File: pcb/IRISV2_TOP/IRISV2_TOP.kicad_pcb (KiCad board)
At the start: 2 copper layers, 50 x 50 mm, 140 parts, among them IC1 ATA6561-GAQW-N, IC2 S25FL256LAGNFI010, IC3 STM32C552MET6, J2 USB_C_Receptacle_USB2.0_16P, J3 USB_C_Receptacle_USB2.0_16P, U4 STM32H563VITx, U5 MMC5983MA, U6 ICM-45686, U7 ICM-45686, U8 BMP581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

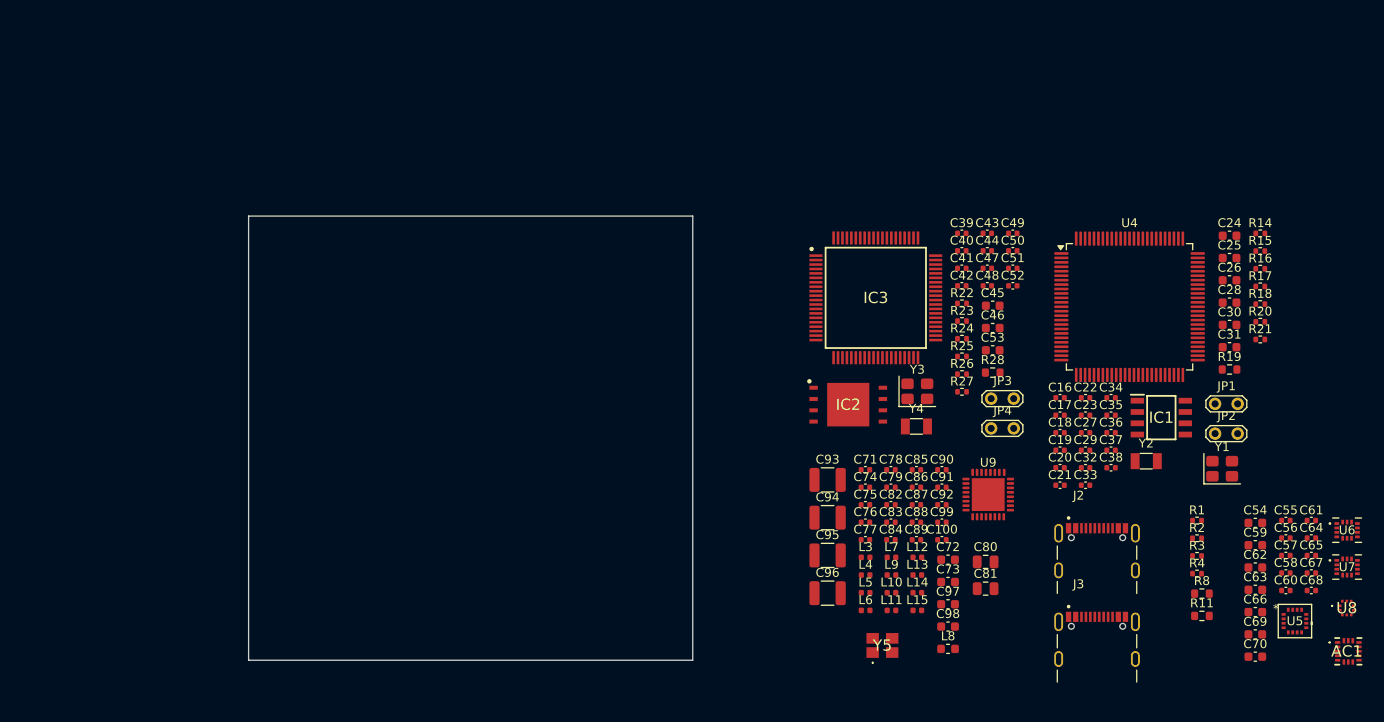
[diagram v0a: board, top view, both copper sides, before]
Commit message: gps finished minus tvs (WHY ARE THEY ALL 0201), top layout + routing started
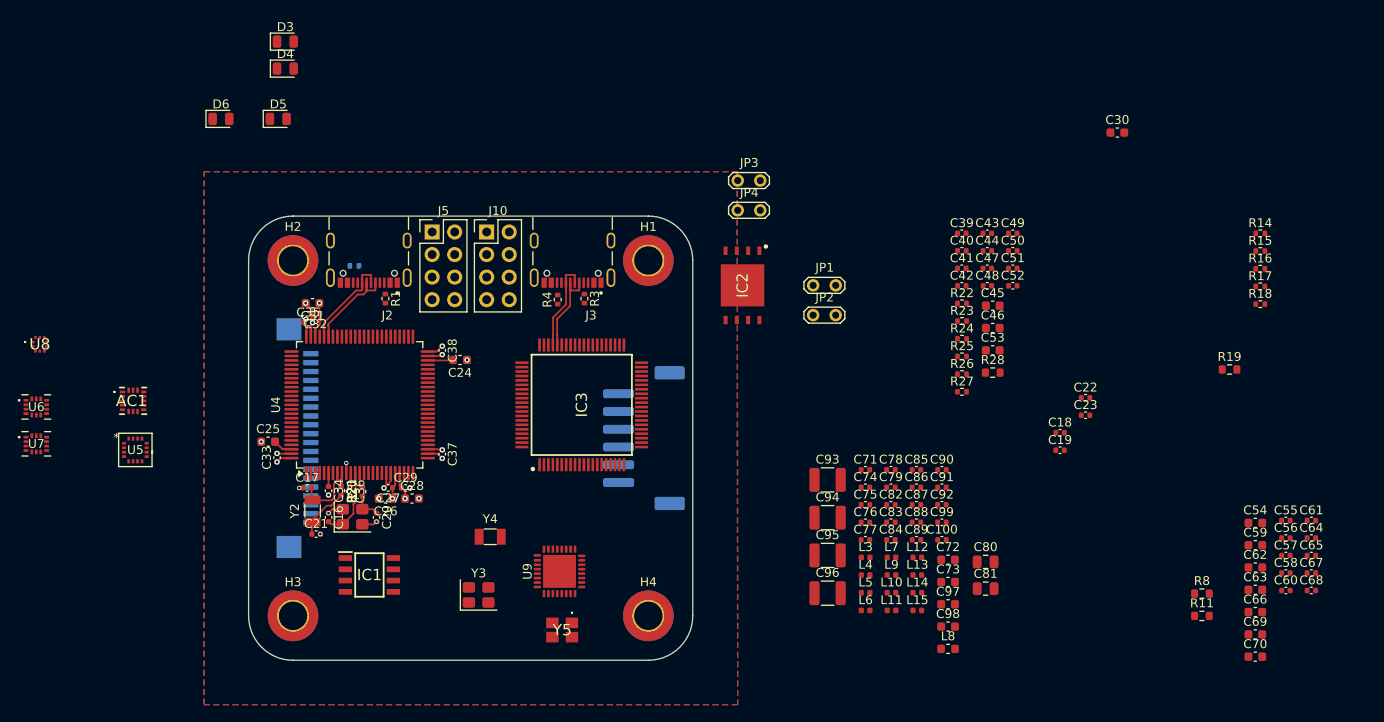
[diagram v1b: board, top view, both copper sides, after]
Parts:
- added D3: 3.3_GOOD, LED_SMD:LED_0805_2012Metric, F.Cu at (129.1, 55.4)
- added D4: 5_GOOD, LED_SMD:LED_0805_2012Metric, F.Cu at (129.1, 58.4)
- added D5: STATUS, LED_SMD:LED_0805_2012Metric, F.Cu at (128.3, 64.1)
- added D6: STATUS, LED_SMD:LED_0805_2012Metric, F.Cu at (121.9, 64.1)
- added H1: MountingHole_Pad, MountingHole:MountingHole_3.2mm_M3_ISO7380_Pad_TopBottom, F.Cu at (170.0, 80.0)
- added H2: MountingHole_Pad, MountingHole:MountingHole_3.2mm_M3_ISO7380_Pad_TopBottom, F.Cu at (130.0, 80.0)
- added H3: MountingHole_Pad, MountingHole:MountingHole_3.2mm_M3_ISO7380_Pad_TopBottom, F.Cu at (130.0, 120.0)
- added H4: MountingHole_Pad, MountingHole:MountingHole_3.2mm_M3_ISO7380_Pad_TopBottom, F.Cu at (170.0, 120.0)
- added J1: Conn_01x20_MountingPin, FFC3B07-20-T:FFC3B07-20-T, B.Cu at (132.0, 100.0)
- added J10: Conn_02x04_Odd_Even, Connector_PinHeader_2.54mm:PinHeader_2x04_P2.54mm_Vertical, F.Cu at (151.8, 76.8)
- added J5: Conn_02x04_Odd_Even, Connector_PinHeader_2.54mm:PinHeader_2x04_P2.54mm_Vertical, F.Cu at (145.7, 76.8)
- added J9: Conn_01x06_MountingPin, Connector_JST:JST_PH_S6B-PH-SM4-TB_1x06-1MP_P2.00mm_Horizontal, B.Cu at (169.5, 100.0)
- R2: moved to B.Cu
- moved U8 150.1 mm to (101.5, 89.4)
- moved U6 148.2 mm to (101.1, 96.5)
- moved U7 148.2 mm to (101.1, 100.6)
- moved AC1 139.7 mm to (112.0, 95.8)
- moved U5 132.0 mm to (112.2, 101.3)
- moved C25 110.2 mm to (127.2, 100.4)
- moved R21 104.9 mm to (135.4, 105.9), turned to -90 degrees
- moved C31 103.3 mm to (132.2, 84.8), turned to 180 degrees
- moved R20 102.9 mm to (137.8, 106.0), turned to 90 degrees
- moved R2 99.7 mm to (136.9, 80.6)
- moved C26 98.1 mm to (140.4, 106.8), turned to 180 degrees
- moved Y1 98.0 mm to (136.7, 108.8)
- moved R1 94.7 mm to (140.4, 84.3), turned to -90 degrees
- moved C28 94.6 mm to (143.4, 106.8)
- moved Y2 94.0 mm to (132.2, 108.2), turned to 90 degrees
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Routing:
- net +3.3V: track 0.00 -> 21.8 mm, vias 0 -> 8
- net GND: track 0.00 -> 20.8 mm, vias 0 -> 18
- net usb1_d+: track 0.00 -> 10.9 mm
- net usb1_d-: track 0.00 -> 10.9 mm
- net usb2_d+: track 0.00 -> 10.3 mm
- net usb2_d-: track 0.00 -> 10.3 mm
- net /main_mcu/hse_0: track 0.00 -> 8.12 mm
- net /main_mcu/lse_0: track 0.00 -> 6.91 mm
- net /main_mcu/lse_1: track 0.00 -> 6.49 mm
- net Net-(C24-Pad2): track 0.00 -> 5.07 mm
- net /main_mcu/hse_1: track 0.00 -> 3.27 mm
- net Net-(U4-PH1): track 0.00 -> 1.69 mm
- net Net-(U4-PC15): track 0.00 -> 1.52 mm
- added copper zone on In2.Cu, net +3.3V
- added copper zone on B.Cu, net GND
- added copper zone on F.Cu, net GND
- added copper zone on In1.Cu, net GND
- added copper zone on In4.Cu, net GND
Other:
- outline, holes or cut-outs redrawn
- copper layers 2 -> 6

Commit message: removed high g accel, top board layout looking decent, routing started also - though i realized i was missing the micro sd card and that's going to be a pain to add
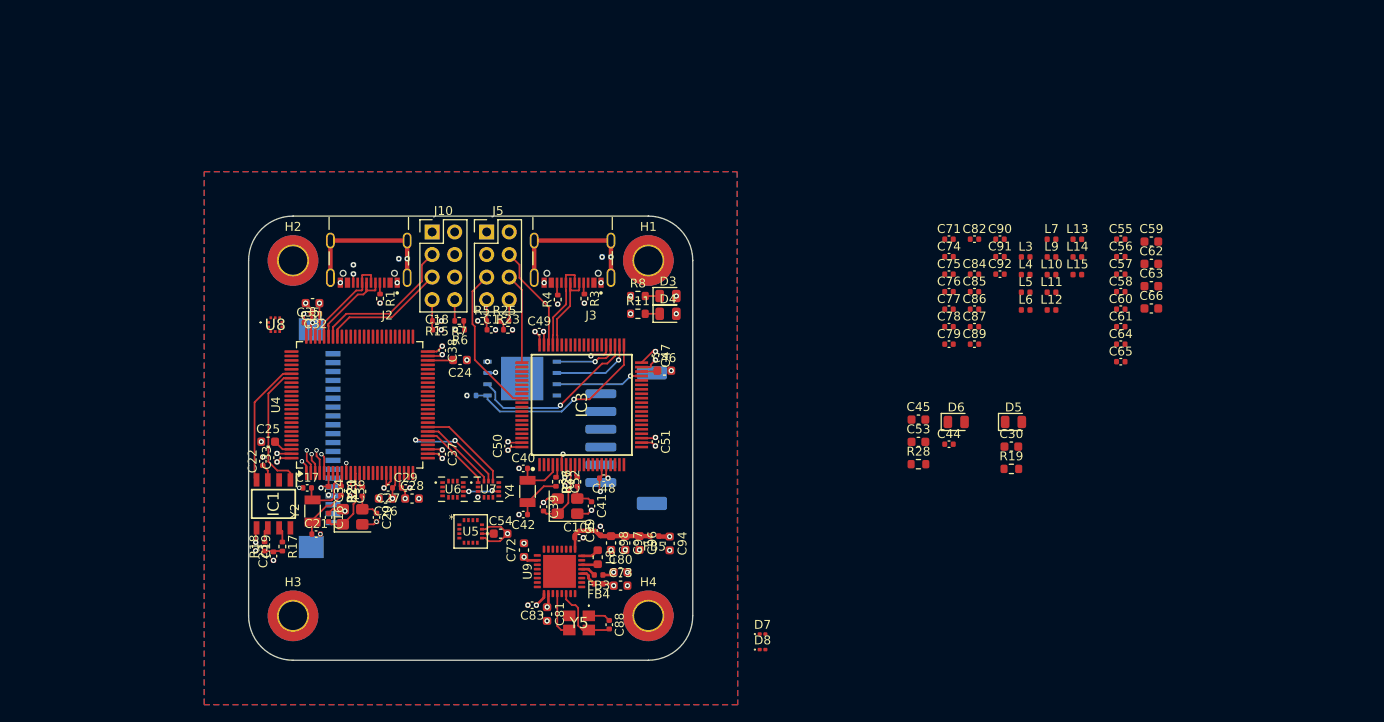
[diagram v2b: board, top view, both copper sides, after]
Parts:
- removed AC1: H3LIS331DLTR, H3LIS331DLTR:LIS3DHTR
- removed C43, C67, C68: 100nF, Capacitor_SMD:C_0402_1005Metric
- removed C69, C70: 10uF, Capacitor_SMD:C_0603_1608Metric
- removed C93, C95: 22uF, Capacitor_SMD:C_1210_3225Metric
- removed JP1, JP3: BOOT, TestPoint:TestPoint_2Pads_Pitch2.54mm_Drill0.8mm
- removed JP2, JP4: RST, TestPoint:TestPoint_2Pads_Pitch2.54mm_Drill0.8mm
- removed R14, R16, R24: 10k, Resistor_SMD:R_0402_1005Metric
- added C1: 100nF, Capacitor_SMD:C_0402_1005Metric, F.Cu at (152.3, 87.8)
- added D7: D_TVS, Diode_SMD:D_0201_0603Metric, F.Cu at (182.9, 122.0)
- added D8: D_TVS, Diode_SMD:D_0201_0603Metric, F.Cu at (182.9, 123.8)
- added FB1: FerriteBead_Small, Inductor_SMD:L_0402_1005Metric, B.Cu at (142.4, 79.8)
- added FB2: FerriteBead_Small, Inductor_SMD:L_0402_1005Metric, B.Cu at (165.3, 79.6)
- added FB3: FerriteBead_Small, Inductor_SMD:L_0402_1005Metric, F.Cu at (164.4, 115.4)
- added FB4: FerriteBead_Small, Inductor_SMD:L_0402_1005Metric, F.Cu at (164.4, 116.4)
- added FB5: FerriteBead_Small, Inductor_SMD:L_0402_1005Metric, F.Cu at (170.7, 111.0)
- added R5: 10k, Resistor_SMD:R_0402_1005Metric, F.Cu at (151.3, 86.8)
- added R6: 10k, Resistor_SMD:R_0402_1005Metric, F.Cu at (148.8, 87.8)
- added R7: 10k, Resistor_SMD:R_0402_1005Metric, F.Cu at (148.7, 86.8)
- C80, C81: footprint Capacitor_SMD:C_0805_2012Metric -> Capacitor_SMD:C_0603_1608Metric
- C94: value 22uF -> 1uF; footprint Capacitor_SMD:C_1210_3225Metric -> Capacitor_SMD:C_0603_1608Metric
- C96: value 22uF -> 10uF; footprint Capacitor_SMD:C_1210_3225Metric -> Capacitor_SMD:C_0603_1608Metric
- IC2, R22: moved to B.Cu
- moved R18 115.4 mm to (126.8, 112.2), turned to 90 degrees
- moved R17 113.9 mm to (128.8, 112.2), turned to -90 degrees
- moved R15 93.0 mm to (146.2, 86.8), turned to 180 degrees
- moved C22 92.9 mm to (126.6, 102.6), turned to 90 degrees
- moved C23 92.8 mm to (127.8, 113.3), turned to 90 degrees
- moved C19 91.2 mm to (125.8, 112.2), turned to -90 degrees
- moved D6 89.5 mm to (204.7, 98.2)
- moved D5 89.5 mm to (211.1, 98.2)
- moved C54 85.0 mm to (153.4, 110.8)
- moved R11 72.0 mm to (168.8, 86.0)
- moved R8 71.8 mm to (168.8, 84.0)
- moved C18 71.1 mm to (146.2, 87.8)
- moved C50 60.9 mm to (154.2, 100.9), turned to 90 degrees
- moved C39 56.3 mm to (158.2, 107.7), turned to -90 degrees
- moved R22 56.2 mm to (150.1, 95.2)
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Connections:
- IC3 pad 24: unconnected-(IC3-PA4-Pad24) -> lr_nss
- IC3 pad 33: lr_nss -> unconnected-(IC3-PE7-Pad33)
- IC3 pad 37: ppu_i2c2_scl -> /peripheral_mcu/flash_rst
- IC3 pad 41: ppu_i2c2_sda -> /peripheral_mcu/flash_cs
- IC3 pad 45: unconnected-(IC3-PD12-Pad45) -> /peripheral_mcu/flash_wp
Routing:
- net GND: track 20.8 -> 45.1 mm, vias 18 -> 62
- net /peripheral_mcu/flash_cs: track 0.00 -> 22.1 mm, vias 0 -> 1
- net /peripheral_mcu/flash_miso: track 0.00 -> 19.6 mm, vias 0 -> 1
- net /peripheral_mcu/swo: track 0.00 -> 17.2 mm
- net Net-(J3-SHIELD): track 0.00 -> 17.0 mm, vias 0 -> 1
- net Net-(J2-SHIELD): track 0.00 -> 17.0 mm, vias 0 -> 1
- net /main_mcu/debug_uart_rx: track 0.00 -> 16.7 mm
- net /peripheral_mcu/flash_wp: track 0.00 -> 15.3 mm, vias 0 -> 2
- net /main_mcu/can_tx: track 0.00 -> 14.8 mm
- net +3.3V: track 21.8 -> 36.3 mm, vias 8 -> 21
- net /main_mcu/can_rx: track 0.00 -> 14.3 mm
- net /main_mcu/debug_uart_tx: track 0.00 -> 13.9 mm
- net icm2_sck: track 0.00 -> 12.1 mm, vias 0 -> 2
- net /peripheral_mcu/swdio: track 0.00 -> 12.1 mm
- net /lr2021/lr2021_vbat: track 0.00 -> 10.5 mm
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
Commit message: layout pretty much done, lr2021 rf stuff done, mostly just routing left
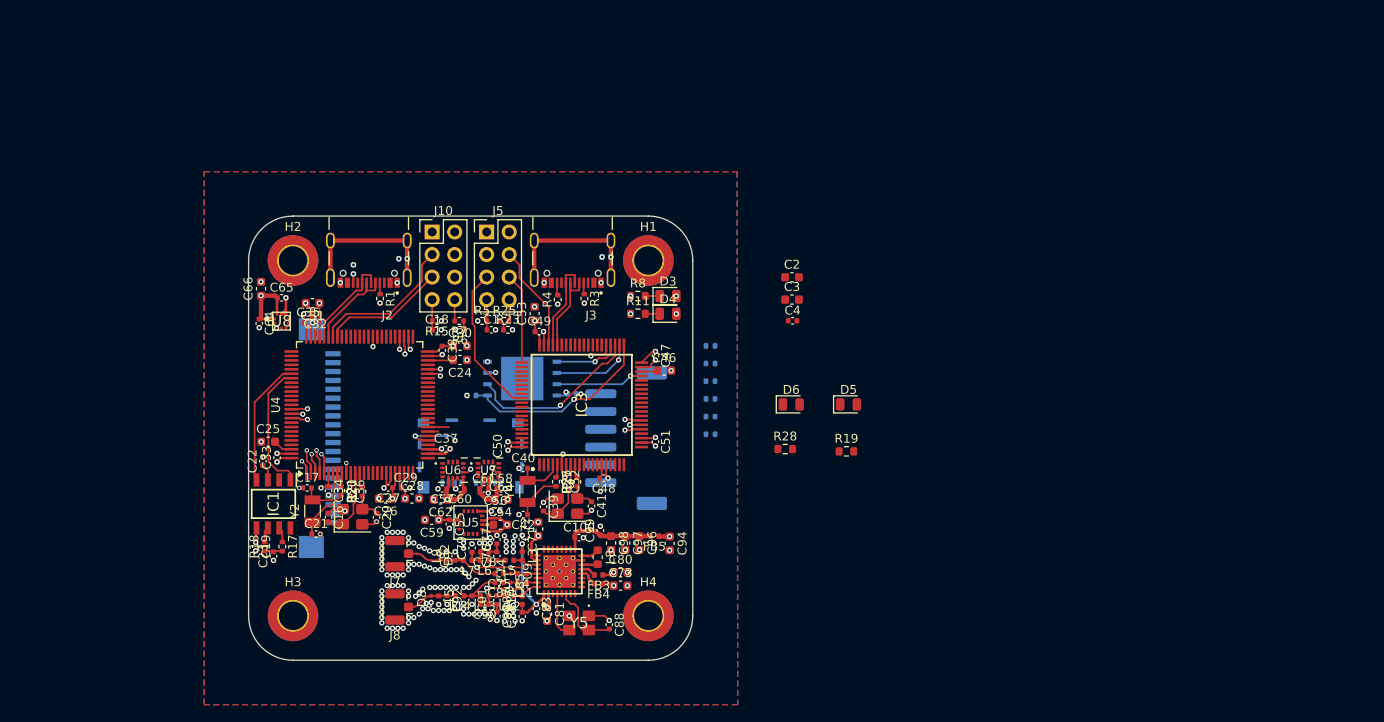
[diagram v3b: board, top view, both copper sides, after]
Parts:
- removed C45: 1uF, Capacitor_SMD:C_0603_1608Metric
- added C2: 10uF, Capacitor_SMD:C_0603_1608Metric, F.Cu at (186.2, 81.9)
- added C3: 1uF, Capacitor_SMD:C_0603_1608Metric, F.Cu at (186.2, 84.4)
- added C4: 100nF, Capacitor_SMD:C_0402_1005Metric, F.Cu at (186.2, 86.8)
- added J6: MEM2085-00-115-00-A, MEM2085-00-115:MEM20850011500A, B.Cu at (150.0, 102.0)
- added J7: Conn_Coaxial, Connector_Coaxial:U.FL_Hirose_U.FL-R-SMT-1_Vertical, F.Cu at (141.9, 113.0)
- added J8: Conn_Coaxial, Connector_Coaxial:U.FL_Hirose_U.FL-R-SMT-1_Vertical, F.Cu at (141.9, 119.0)
- added R10: 10k, Resistor_SMD:R_0402_1005Metric, B.Cu at (177.0, 91.6)
- added R12: 10k, Resistor_SMD:R_0402_1005Metric, B.Cu at (177.0, 93.6)
- added R13: 10k, Resistor_SMD:R_0402_1005Metric, B.Cu at (177.0, 95.6)
- added R14: 10k, Resistor_SMD:R_0402_1005Metric, B.Cu at (177.0, 97.6)
- added R16: 10k, Resistor_SMD:R_0402_1005Metric, B.Cu at (177.0, 99.6)
- added R9: 10k, Resistor_SMD:R_0402_1005Metric, B.Cu at (177.0, 89.6)
- C44: moved to B.Cu
- C74, C85: footprint Capacitor_SMD:C_0402_1005Metric -> Capacitor_SMD:C_0201_0603Metric
- U9: footprint LR2021:LR2021 -> LR2021:LR2021_thermalvias
- moved C66 100.2 mm to (126.4, 83.2), turned to 90 degrees
- moved C64 97.0 mm to (126.2, 87.1), turned to -90 degrees
- moved C65 94.7 mm to (128.7, 84.2)
- moved C59 86.8 mm to (145.6, 109.2), turned to 180 degrees
- moved C62 84.3 mm to (146.6, 106.9), turned to 180 degrees
- moved C55 82.1 mm to (147.6, 109.7), turned to -90 degrees
- moved L15 80.7 mm to (146.4, 118.2), turned to -90 degrees
- moved C57 80.1 mm to (146.8, 105.7), turned to 180 degrees
- moved L14 79.3 mm to (148.8, 117.8), turned to 180 degrees
- moved L13 77.9 mm to (151.6, 117.8), turned to 180 degrees
- moved C60 77.1 mm to (148.8, 105.7), turned to 180 degrees
- moved C63 77.1 mm to (153.4, 106.9)
- moved C56 76.0 mm to (152.8, 108.2)
- moved L9 76.0 mm to (147.3, 113.3), turned to 90 degrees
- moved L7 75.0 mm to (149.7, 113.8), turned to 180 degrees
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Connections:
- net Net-(D7-A2) renamed /lr2021/lf
- C86 pad 2: Net-(D8-A2) -> /lr2021/hf_tiein
- C90 pad 2: Net-(C90-Pad2) -> /lr2021/hf_tiein
- C91 pad 1: Net-(C90-Pad2) -> /lr2021/hf_tiein
- C92 pad 1: Net-(D8-A2) -> /lr2021/hf
- D8 pad 2: Net-(D8-A2) -> /lr2021/hf
- IC3 pad 33: unconnected-(IC3-PE7-Pad33) -> /peripheral_mcu/sd_cs
- L13 pad 2: Net-(C90-Pad2) -> /lr2021/hf_tiein
- L14 pad 1: Net-(C90-Pad2) -> /lr2021/hf_tiein
- L14 pad 2: Net-(D8-A2) -> /lr2021/hf
- L15 pad 1: Net-(D8-A2) -> /lr2021/hf
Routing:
- net mcu->ppu_sck: track 0.00 -> 40.5 mm, vias 0 -> 2
- net mcu->ppu_miso: track 0.00 -> 39.7 mm, vias 0 -> 2
- net mcu->ppu_mosi: track 0.00 -> 39.7 mm, vias 0 -> 2
- net +3.3V: track 36.3 -> 66.7 mm, vias 21 -> 27
- net GND: track 45.1 -> 68.3 mm, vias 62 -> 205
- net /lr2021/lr2021_vdcc: track 2.95 -> 19.3 mm
- net /lr2021/vr_pa: track 1.65 -> 12.8 mm, vias 1 -> 2
- net /lr2021/lf: track 0.00 -> 10.5 mm
- net /lr2021/lr2021_vpax: track 2.93 -> 12.0 mm
- net icm2_cs: track 10.5 -> 2.40 mm
- net icm2_mosi: track 8.91 -> 1.20 mm
- net icm2_miso: track 8.18 -> 0.99 mm
- net /lr2021/hf_tiein: track 0.00 -> 5.95 mm
- net icm2_sck: track 12.1 -> 6.31 mm
- net /lr2021/hf: track 0.00 -> 5.70 mm
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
